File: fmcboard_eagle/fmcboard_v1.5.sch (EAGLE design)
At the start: 184 parts, among them IC1 OPA699ID, IC10 LTC6229IMS8E#TRPBF, IC11 7805TV, IC12 SN74AUC2G66DCTR, IC13 SN74AUC2G66DCTR, IC14 SN74AUC2G66DCTR, IC15 SN74AUC2G66DCTR, IC16 DAC7578SPWR, IC17 SN74AUC2G66DCTR, IC18 SN74AUC2G66DCTR, IC19 SN74AUC2G66DCTR, IC2 DAC7578SPWR, IC20 SN74AUC2G66DCTR, IC21 74AUP2GU04GW,125, IC22 74AUP2GU04GW,125, IC23 74AUP2GU04GW,125, IC24 74AUP2GU04GW,125, IC25 LM358, IC3 LTC6229IMS8E#TRPBF, IC4 LTC6229IMS8E#TRPBF, IC6 OPA699ID, IC7 OPA699ID, IC8 LTC6229IMS8E#TRPBF, IC9 LTC6229IMS8E#TRPBF, J1 8pin, J10 8pin, J12 4p-2.54, J2 ASP-134604-01, J3 4p-2.54, J4 4p-2.54, J5 8pin, J6 4p-2.54, J7 4p-2.54, J8 4p-2.54, J9 8pin, U1 TXS0108EPWR, U2 STMICROELECTRONICS_L7905ACVST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

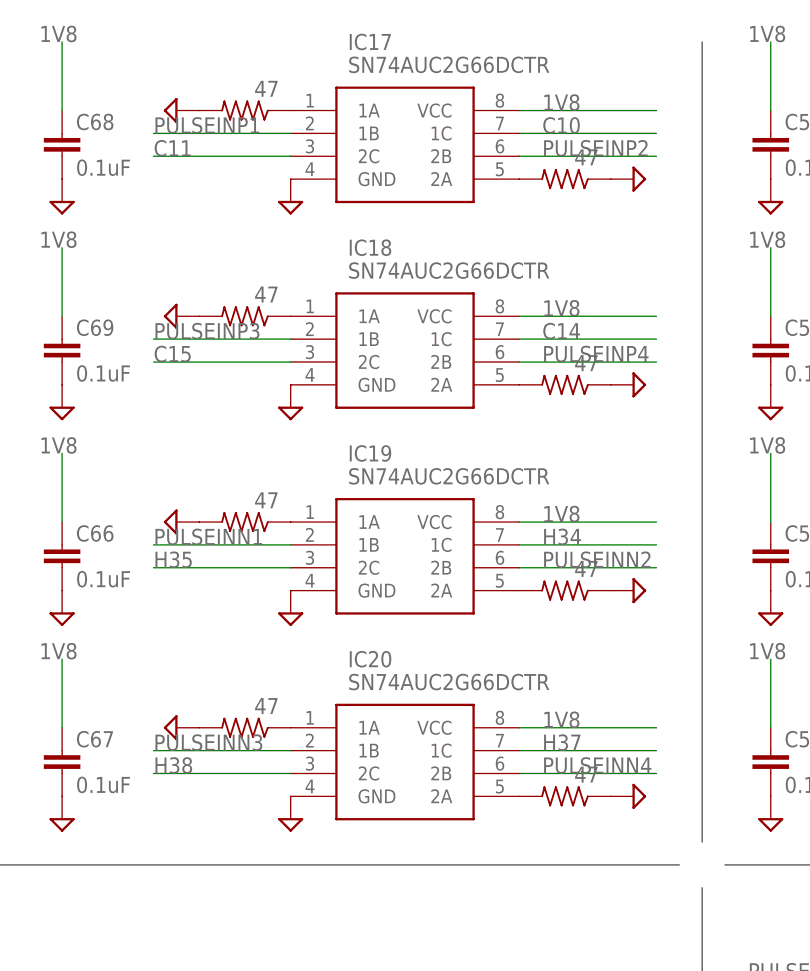
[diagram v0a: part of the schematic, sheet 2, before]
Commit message: remove 47 ohm resistors to gnd
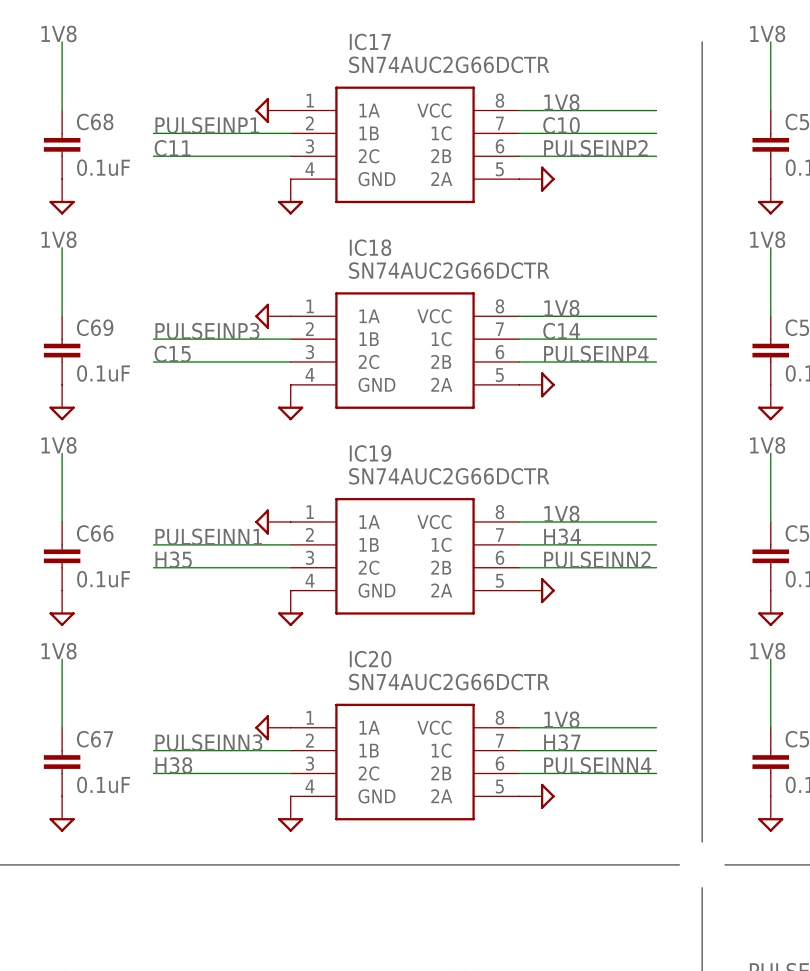
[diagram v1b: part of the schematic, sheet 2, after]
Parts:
- removed R37, R39, R41, R43, R44, R45, R46, R52: 47, rcl:R-US_R0805
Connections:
- removed net N$15: IC19.2A, R41.2
- removed net N$16: IC20.2A, R43.2
- removed net N$17: IC20.1A, R44.1
- removed net N$19: IC19.1A, R45.1
- removed net N$20: IC18.1A, R46.1
- removed net N$5: IC17.1A, R52.1
- removed net N$6: IC17.2A, R37.2
- removed net N$7: IC18.2A, R39.2
- net GND: now also IC17.1A, IC17.2A, IC18.1A, IC18.2A, IC19.1A, IC19.2A, IC20.1A, IC20.2A; no longer R37.1, R39.1, R41.1, R43.1, R44.2, R45.2, R46.2, R52.2
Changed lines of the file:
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@@
 <part name="C40" library="SparkFun-Passives" deviceset="CAP" device="0805" value="10uF"/>
 <part name="C41" library="SparkFun-Passives" deviceset="CAP" device="0805" value="10uF"/>
-<part name="R52" library="rcl" library_urn="urn:adsk.eagle:library:334" deviceset="R-US_" device="R0805" package3d_urn="urn:adsk.eagle:package:23553/2" value="47"/>
 <part name="C56" library="SparkFun-Passives" deviceset="CAP" device="0805" value="1uF"/>
 <part name="C57" library="SparkFun-Passives" deviceset="CAP" device="0805" value="1uF"/>
@@
 <part name="IC19" library="SN74AUC2G66DCTR" deviceset="SN74AUC2G66DCTR" device=""/>
 <part name="IC20" library="SN74AUC2G66DCTR" deviceset="SN74AUC2G66DCTR" device=""/>
-<part name="R37" library="rcl" library_urn="urn:adsk.eagle:library:334" deviceset="R-US_" device="R0805" package3d_urn="urn:adsk.eagle:package:23553/2" value="47"/>
-<part name="R39" library="rcl" library_urn="urn:adsk.eagle:library:334" deviceset="R-US_" device="R0805" package3d_urn="urn:adsk.eagle:package:23553/2" value="47"/>
-<part name="R41" library="rcl" library_urn="urn:adsk.eagle:library:334" deviceset="R-US_" device="R0805" package3d_urn="urn:adsk.eagle:package:23553/2" value="47"/>
-<part name="R43" library="rcl" library_urn="urn:adsk.eagle:library:334" deviceset="R-US_" device="R0805" package3d_urn="urn:adsk.eagle:package:23553/2" value="47"/>
-<part name="R44" library="rcl" library_urn="urn:adsk.eagle:library:334" deviceset="R-US_" device="R0805" package3d_urn="urn:adsk.eagle:package:23553/2" value="47"/>
-<part name="R45" library="rcl" library_urn="urn:adsk.eagle:library:334" deviceset="R-US_" device="R0805" package3d_urn="urn:adsk.eagle:package:23553/2" value="47"/>
-<part name="R46" library="rcl" library_urn="urn:adsk.eagle:library:334" deviceset="R-US_" device="R0805" package3d_urn="urn:adsk.eagle:package:23553/2" value="47"/>
 <part name="SUPPLY73" library="supply2" library_urn="urn:adsk.eagle:library:372" deviceset="GND" device=""/>
 <part name="SUPPLY74" library="supply2" library_urn="urn:adsk.eagle:library:372" deviceset="GND" device=""/>
@@
 <text x="-15.24" y="119.38" size="1.778" layer="90">Pulse switches to gnd</text>
 <wire x1="-66.04" y1="30.48" x2="-66.04" y2="119.38" width="0.1524" layer="97"/>
-<text x="-68.58" y="20.32" size="1.778" layer="90">Inverters for pulse
-switches to DACs</text>
+<text x="-63.5" y="22.86" size="1.778" layer="90">Inverters for pulse switches to DACs</text>
 <wire x1="12.7" y1="-22.86" x2="12.7" y2="25.4" width="0.1524" layer="97"/>
 <wire x1="10.16" y1="27.94" x2="-71.12" y2="27.94" width="0.1524" layer="97"/>
@@
 <instance part="SUPPLY75" gate="GND" x="124.46" y="-30.48" smashed="yes"/>
 <instance part="SUPPLY76" gate="GND" x="226.06" y="-30.48" smashed="yes"/>
-<instance part="R52" gate="G$1" x="-38.1" y="111.76" smashed="yes" rot="R180">
-<attribute name="VALUE" x="-34.29" y="115.062" size="1.778" layer="96" rot="R180"/>
-</instance>
 <instance part="C56" gate="G$1" x="132.08" y="-7.62" smashed="yes" rot="R90">
 <attribute name="VALUE" x="133.096" y="-5.461" size="1.778" layer="96" rot="R180"/>
@@
 <attribute name="VALUE" x="-26.67" y="48.26" size="1.778" layer="96" align="center-left"/>
 </instance>
-<instance part="R37" gate="G$1" x="-2.54" y="104.14" smashed="yes" rot="R180">
-<attribute name="VALUE" x="1.27" y="107.442" size="1.778" layer="96" rot="R180"/>
-</instance>
-<instance part="R39" gate="G$1" x="-2.54" y="81.28" smashed="yes" rot="R180">
-<attribute name="VALUE" x="1.27" y="84.582" size="1.778" layer="96" rot="R180"/>
-</instance>
-<instance part="R41" gate="G$1" x="-2.54" y="58.42" smashed="yes" rot="R180">
-<attribute name="VALUE" x="1.27" y="61.722" size="1.778" layer="96" rot="R180"/>
-</instance>
-<instance part="R43" gate="G$1" x="-2.54" y="35.56" smashed="yes" rot="R180">
-<attribute name="VALUE" x="1.27" y="38.862" size="1.778" layer="96" rot="R180"/>
-</instance>
-<instance part="R44" gate="G$1" x="-38.1" y="43.18" smashed="yes" rot="R180">
-<attribute name="VALUE" x="-34.29" y="46.482" size="1.778" layer="96" rot="R180"/>
-</instance>
-<instance part="R45" gate="G$1" x="-38.1" y="66.04" smashed="yes" rot="R180">
-<attribute name="VALUE" x="-34.29" y="69.342" size="1.778" layer="96" rot="R180"/>
-</instance>
-<instance part="R46" gate="G$1" x="-38.1" y="88.9" smashed="yes" rot="R180">
-<attribute name="VALUE" x="-34.29" y="92.202" size="1.778" layer="96" rot="R180"/>
-</instance>
-<instance part="SUPPLY73" gate="GND" x="-45.72" y="111.76" smashed="yes" rot="R270"/>
-<instance part="SUPPLY74" gate="GND" x="-45.72" y="88.9" smashed="yes" rot="R270"/>
-<instance part="SUPPLY77" gate="GND" x="-45.72" y="66.04" smashed="yes" rot="R270"/>
-<instance part="SUPPLY78" gate="GND" x="-45.72" y="43.18" smashed="yes" rot="R270"/>
-<instance part="SUPPLY79" gate="GND" x="5.08" y="35.56" smashed="yes" rot="R90"/>
-<instance part="SUPPLY80" gate="GND" x="5.08" y="58.42" smashed="yes" rot="R90"/>
-<instance part="SUPPLY81" gate="GND" x="5.08" y="81.28" smashed="yes" rot="R90"/>
-<instance part="SUPPLY82" gate="GND" x="5.08" y="104.14" smashed="yes" rot="R90"/>
+<instance part="SUPPLY73" gate="GND" x="-35.56" y="111.76" smashed="yes" rot="R270"/>
+<instance part="SUPPLY74" gate="GND" x="-35.56" y="88.9" smashed="yes" rot="R270"/>
+<instance part="SUPPLY77" gate="GND" x="-35.56" y="66.04" smashed="yes" rot="R270"/>
+<instance part="SUPPLY78" gate="GND" x="-35.56" y="43.18" smashed="yes" rot="R270"/>
+<instance part="SUPPLY79" gate="GND" x="-5.08" y="35.56" smashed="yes" rot="R90"/>
+<instance part="SUPPLY80" gate="GND" x="-5.08" y="58.42" smashed="yes" rot="R90"/>
+<instance part="SUPPLY81" gate="GND" x="-5.08" y="81.28" smashed="yes" rot="R90"/>
+<instance part="SUPPLY82" gate="GND" x="-5.08" y="104.14" smashed="yes" rot="R90"/>
 <instance part="IC21" gate="G$1" x="-63.5" y="7.62" smashed="yes">
 <attribute name="NAME" x="-59.69" y="15.24" size="1.778" layer="95" align="center-left"/>
@@
 </segment>
 <segment>
-<pinref part="R52" gate="G$1" pin="2"/>
-<pinref part="SUPPLY73" gate="GND" pin="GND"/>
-</segment>
-<segment>
-<pinref part="R46" gate="G$1" pin="2"/>
-<pinref part="SUPPLY74" gate="GND" pin="GND"/>
-</segment>
-<segment>
-<pinref part="R45" gate="G$1" pin="2"/>
-<pinref part="SUPPLY77" gate="GND" pin="GND"/>
-</segment>
-<segment>
-<pinref part="R44" gate="G$1" pin="2"/>
-<pinref part="SUPPLY78" gate="GND" pin="GND"/>
-</segment>
-<segment>
-<pinref part="R43" gate="G$1" pin="1"/>
-<pinref part="SUPPLY79" gate="GND" pin="GND"/>
-</segment>
-<segment>
-<pinref part="R41" gate="G$1" pin="1"/>
-<pinref part="SUPPLY80" gate="GND" pin="GND"/>
-</segment>
-<segment>
-<pinref part="R39" gate="G$1" pin="1"/>
-<pinref part="SUPPLY81" gate="GND" pin="GND"/>
-</segment>
-<segment>
-<pinref part="R37" gate="G$1" pin="1"/>
-<pinref part="SUPPLY82" gate="GND" pin="GND"/>
-</segment>
-<segment>
 <pinref part="IC21" gate="G$1" pin="GND"/>
 <pinref part="SUPPLY83" gate="GND" pin="GND"/>
@@
 <pinref part="C71" gate="G$1" pin="2"/>
 <pinref part="SUPPLY92" gate="GND" pin="GND"/>
+</segment>
+<segment>
+<pinref part="IC17" gate="G$1" pin="1A"/>
+<pinref part="SUPPLY73" gate="GND" pin="GND"/>
+</segment>
+<segment>
+<pinref part="IC17" gate="G$1" pin="2A"/>
+<pinref part="SUPPLY82" gate="GND" pin="GND"/>
+</segment>
+<segment>
+<pinref part="IC18" gate="G$1" pin="2A"/>
+<pinref part="SUPPLY81" gate="GND" pin="GND"/>
+</segment>
+<segment>
+<pinref part="IC19" gate="G$1" pin="2A"/>
+<pinref part="SUPPLY80" gate="GND" pin="GND"/>
+</segment>
+<segment>
+<pinref part="IC20" gate="G$1" pin="2A"/>
+<pinref part="SUPPLY79" gate="GND" pin="GND"/>
+</segment>
+<segment>
+<pinref part="IC18" gate="G$1" pin="1A"/>
+<pinref part="SUPPLY74" gate="GND" pin="GND"/>
+</segment>
+<segment>
+<pinref part="IC19" gate="G$1" pin="1A"/>
+<pinref part="SUPPLY77" gate="GND" pin="GND"/>
+</segment>
+<segment>
+<pinref part="IC20" gate="G$1" pin="1A"/>
+<pinref part="SUPPLY78" gate="GND" pin="GND"/>
 </segment>
 </net>
@@
 </segment>
 </net>
-<net name="N$5" class="0">
-<segment>
-<pinref part="IC17" gate="G$1" pin="1A"/>
-<pinref part="R52" gate="G$1" pin="1"/>
-</segment>
-</net>
-<net name="N$6" class="0">
-<segment>
-<pinref part="IC17" gate="G$1" pin="2A"/>
-<pinref part="R37" gate="G$1" pin="2"/>
-</segment>
-</net>
-<net name="N$7" class="0">
-<segment>
-<pinref part="IC18" gate="G$1" pin="2A"/>
-<pinref part="R39" gate="G$1" pin="2"/>
-</segment>
-</net>
-<net name="N$15" class="0">
-<segment>
-<pinref part="IC19" gate="G$1" pin="2A"/>
-<pinref part="R41" gate="G$1" pin="2"/>
-</segment>
-</net>
-<net name="N$16" class="0">
-<segment>
-<pinref part="IC20" gate="G$1" pin="2A"/>
-<pinref part="R43" gate="G$1" pin="2"/>
-</segment>
-</net>
-<net name="N$17" class="0">
-<segment>
-<pinref part="IC20" gate="G$1" pin="1A"/>
-<pinref part="R44" gate="G$1" pin="1"/>
-</segment>
-</net>
-<net name="N$19" class="0">
-<segment>
-<pinref part="IC19" gate="G$1" pin="1A"/>
-<pinref part="R45" gate="G$1" pin="1"/>
-</segment>
-</net>
-<net name="N$20" class="0">
-<segment>
-<pinref part="IC18" gate="G$1" pin="1A"/>
-<pinref part="R46" gate="G$1" pin="1"/>
-</segment>
-</net>
